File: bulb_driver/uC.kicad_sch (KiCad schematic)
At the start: 0 parts

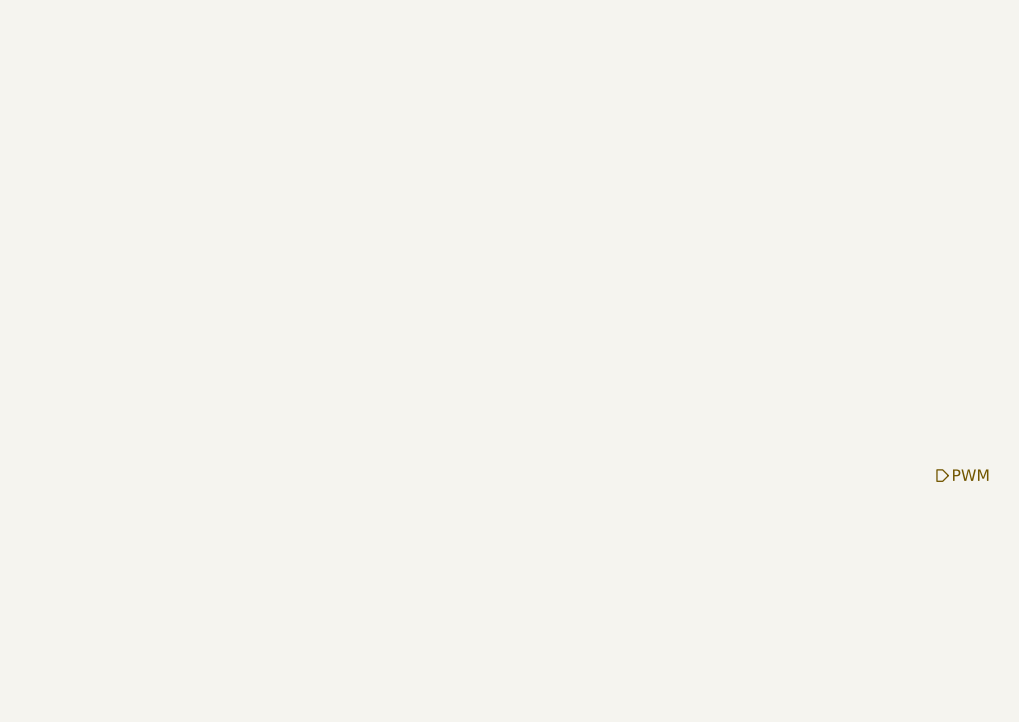
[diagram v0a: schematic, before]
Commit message: Project update
Add USB and Touch sheets

Make initial schematic for uC block
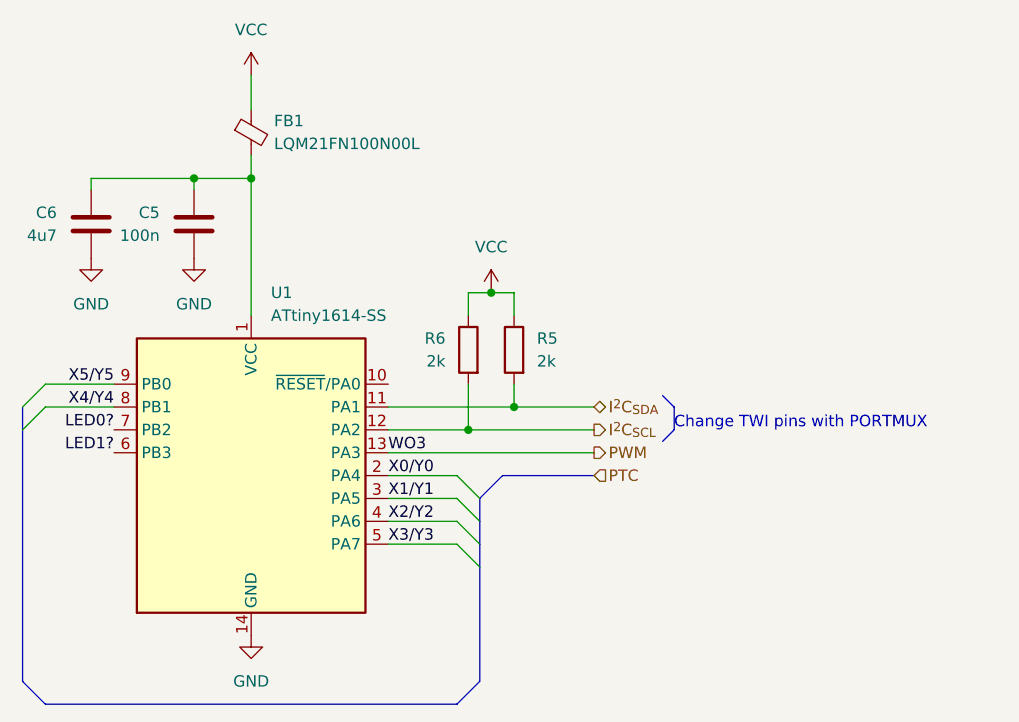
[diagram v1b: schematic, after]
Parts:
- added C5: 100n, symbol Device:C
- added C6: 4u7, symbol Device:C
- added FB1: LQM21FN100N00L, symbol Device:FerriteBead_Small
- added R5, R6: 2k, symbol Device:R
- added U1: ATtiny1614-SS, Package_SO:SOIC-14_3.9x8.7mm_P1.27mm, symbol MCU_Microchip_ATtiny:ATtiny1614-SS
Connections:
- net PWM: now also U1.13 (PA3)
- new net: C5.1, C6.1, FB1.2, U1.1 (VCC)
- new net GND: C5.2, C6.2, U1.14 (GND)
- new net I^{2}C_{SCL}: R6.2, U1.12 (PA2)
- new net I^{2}C_{SDA}: R5.2, U1.11 (PA1)
- new net LED0?: U1.7 (PB2)
- new net LED1?: U1.6 (PB3)
- new net VCC: FB1.1, R5.1, R6.1
- new net X0/Y0: U1.2 (PA4)
- new net X1/Y1: U1.3 (PA5)
- new net X2/Y2: U1.4 (PA6)
- new net X3/Y3: U1.5 (PA7)
- new net X4/Y4: U1.8 (PB1)
- new net X5/Y5: U1.9 (PB0)
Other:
- note added: "Change TWI pins with PORTMUX"
